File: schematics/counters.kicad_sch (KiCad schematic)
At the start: 50 parts, among them Q1 S8050, U1 74HC14, U10 74HC390, U3 74HC86, U4 74HC4046, U5 74HC390, U6 74HC390, U7 74HC390, U8 LMC555xN, U9 74HC390

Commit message: preliminary PCB design
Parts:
- removed D10, D11, D12, D13, D14, D15, D16, D17, D18, D19, D20, D21, D22, D9: 1N4148, Diode_THT:D_DO-35_SOD27_P7.62mm_Horizontal, symbol Diode:1N4148
- removed R15: 4K7, Resistor_THT:R_Axial_DIN0207_L6.3mm_D2.5mm_P7.62mm_Horizontal, symbol Device:R
- removed R16: 10K, Resistor_THT:R_Axial_DIN0207_L6.3mm_D2.5mm_P7.62mm_Horizontal, symbol Device:R
- removed R17: 1K, Resistor_THT:R_Axial_DIN0207_L6.3mm_D2.5mm_P7.62mm_Horizontal, symbol Device:R
- removed RN2: 4K7, Resistor_THT:R_Array_SIP9, symbol Device:R_Network08_Split
- added C31, C32: 100N, bvclock:THT_Cap, symbol Device:C
- added U31, U33: 74HC08, Package_DIP:DIP-14_W7.62mm, symbol 74xx:74LS08
- added U32: 74HC32, Package_DIP:DIP-14_W7.62mm, symbol 74xx:74LS32
- C10, C11, C12, C13, C14, C15, C16, C17, C18, C19, C8, C9: footprint Capacitor_THT:C_Disc_D5.1mm_W3.2mm_P5.00mm -> bvclock:THT_Cap
- D8: footprint Diode_THT:D_DO-35_SOD27_P7.62mm_Horizontal -> bvclock:THT_D_Vertical
- Q1: value S8050 -> 2N2222
- R10, R11, R12, R13, R7, R8, R9: footprint Resistor_THT:R_Axial_DIN0207_L6.3mm_D2.5mm_P7.62mm_Horizontal -> bvclock:THT_R_Vertical
- R14: value 100R -> 82R; footprint Resistor_THT:R_Axial_DIN0207_L6.3mm_D2.5mm_P7.62mm_Horizontal -> bvclock:THT_R_Vertical
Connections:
- net +3V3: now also R11.2, C31.1, C32.1, U31.14 (VCC), U33.14 (VCC); no longer R11.1
- net GND: now also R8.1, R9.1, C31.2, C32.2, U31.7 (GND), U33.1, U33.2, U33.4, U33.5, U33.7 (GND); no longer R8.2, R9.2
- net HADV: now also U33.10
- net HI2: now also U31.5
- net HI4: now also U31.4
- net MADV: now also U33.13
- net MH1: now also U31.1
- net MH2: now also U31.2
- net SH1: now also U31.9
- net SH2: now also U31.10
- net SRST: now also U32.12
- net at U3.10: now also U33.11
- net at U3.13, U9.14 (2CLR): now also U31.3
- net at U10.13 (2Q_{A}): now also U33.12, U33.9
- net at U3.12: now also U33.8
- net at U10.14 (2CLR), U10.2 (1CLR): now also U31.6
- net at U3.9: now also U31.8, U32.13
- net at RV1.1: now also R11.1; no longer R11.2
- net at D8.1 (K), U1.5: now also R10.1; no longer R10.2
- net at U7.14 (2CLR): now also U32.11
- net at U5.11 (2Q_{B}): now also U31.12
- net at U5.14 (2CLR), U6.1 (1~{CLK}_{A}): now also U31.11
- net at U4.12 (R_{2}): now also R8.2; no longer R8.1
- net at U5.10 (2Q_{C}): now also U31.13
- new net: C8.2, R10.2, R9.2
- no-connect marks 12 -> 14
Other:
- moved on the sheet: C10, C11, C12, C13, C14, C15, C16, C17, C18, C19, C8, C9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

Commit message: fixing DRC violations...
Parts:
- Q1: footprint Package_TO_SOT_THT:TO-92_HandSolder -> bvclock:TO-92_HandSolder
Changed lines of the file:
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@@
 			)
 		)
-		(property "Footprint" "Package_TO_SOT_THT:TO-92_HandSolder"
+		(property "Footprint" "bvclock:TO-92_HandSolder"
 			(at 107.95 135.89 0)
 			(hide yes)

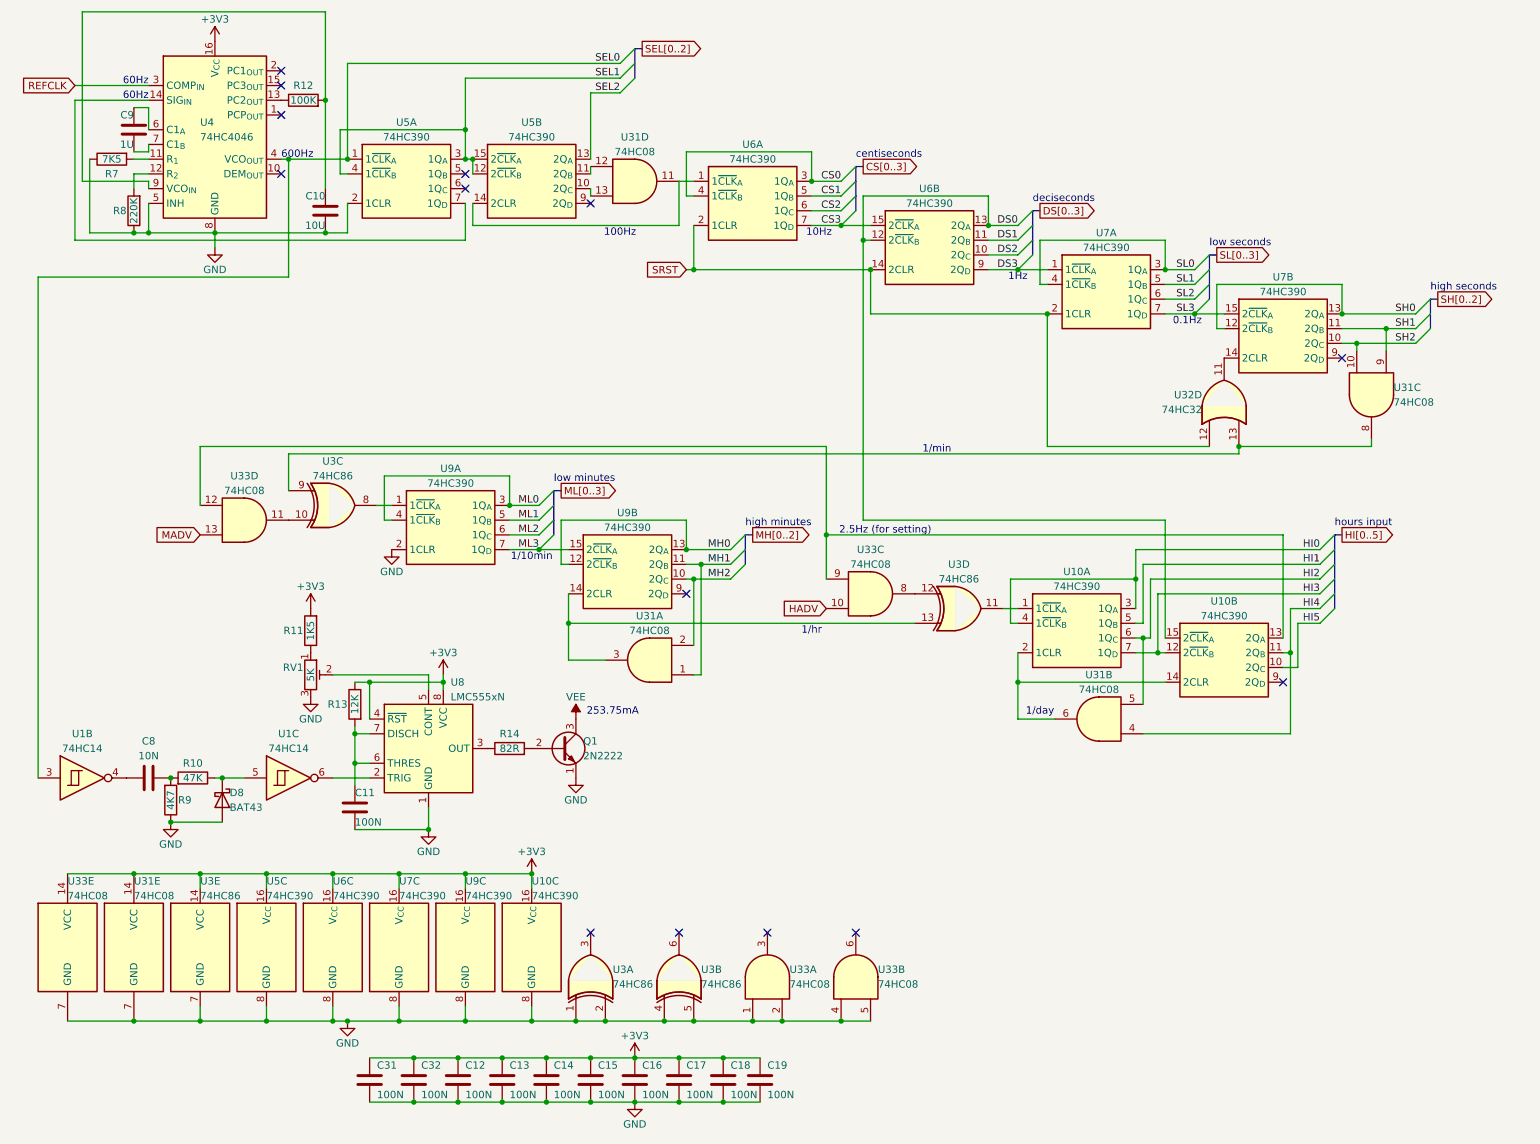
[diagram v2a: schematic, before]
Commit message: passes DRC
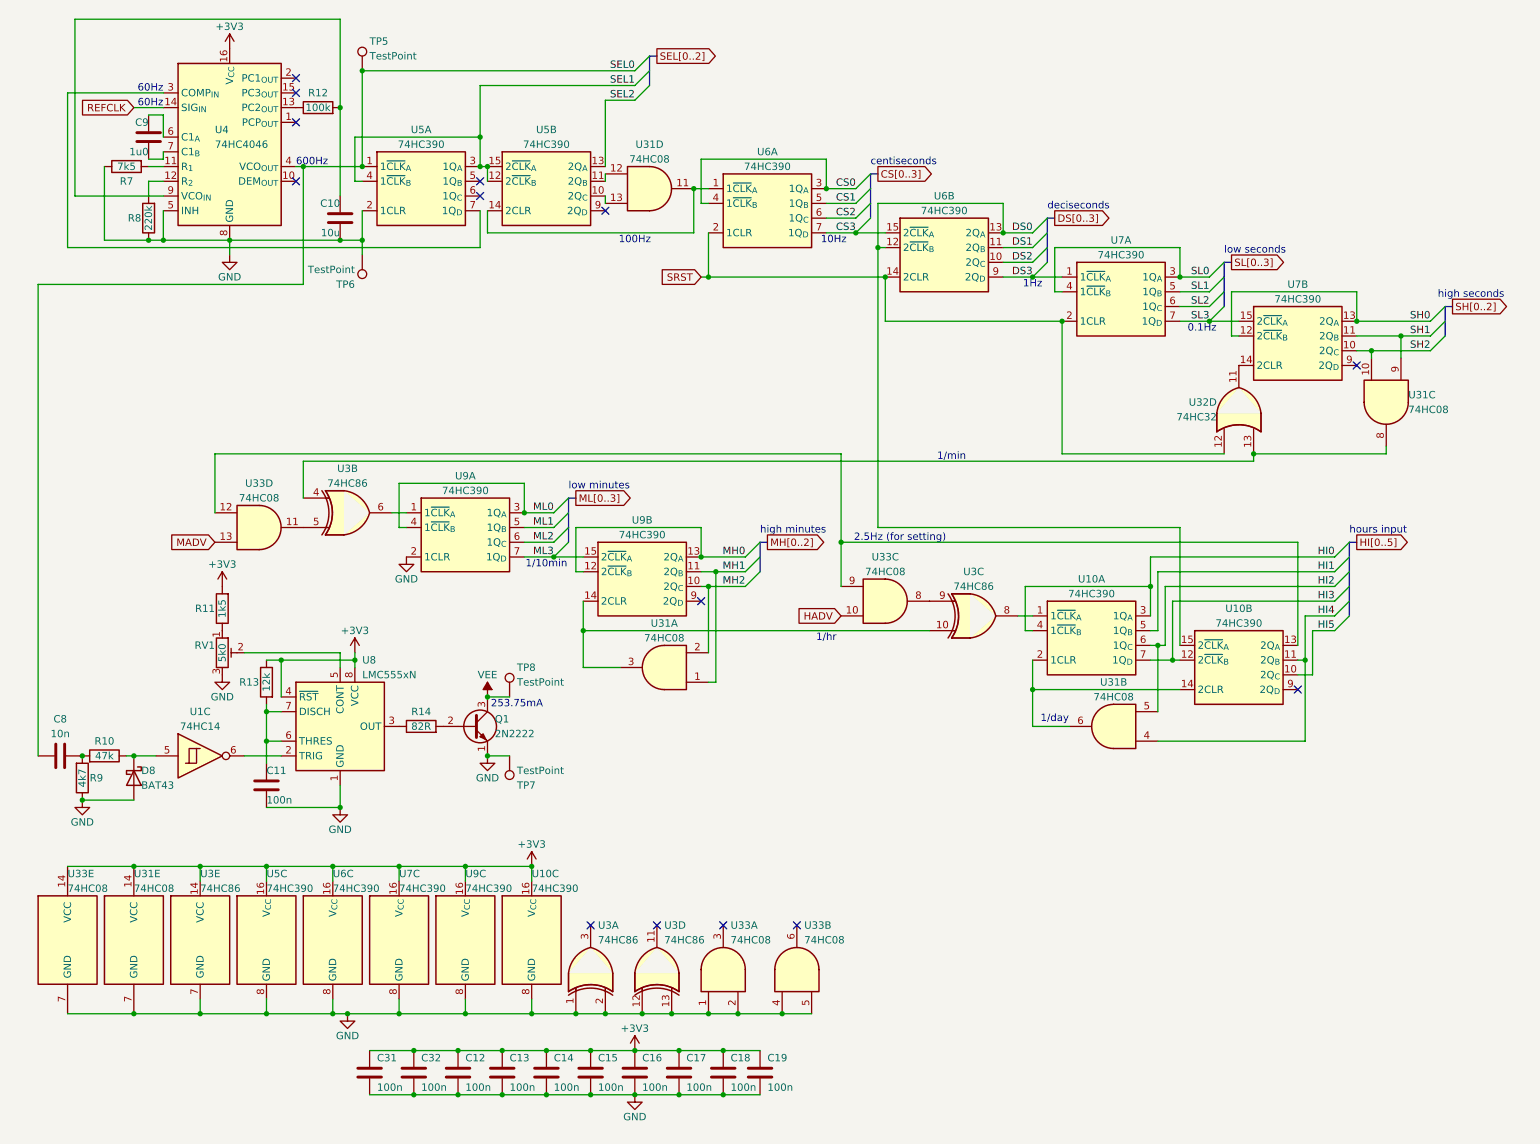
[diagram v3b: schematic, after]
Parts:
- removed unit 2 of U1
- added TP5, TP8: TestPoint, bvclock:TestPoint_THTPad_2.5x2.5mm_Drill1.2mm, symbol Connector:TestPoint
- added TP6, TP7: TestPoint, bvclock:TestPoint_THTPad_D1.0mm_Drill0.5mm, symbol Connector:TestPoint
- C10: value 10U -> 10u
- C11, C12, C13, C14, C15, C16, C17, C18, C19, C31, C32: value 100N -> 100n
- C8: value 10N -> 10n
- C9: value 1U -> 1u0
- R10: value 47K -> 47k
- R11: value 1K5 -> 1k5
- R12: value 100K -> 100k
- R13: value 12K -> 12k
- R7: value 7K5 -> 7k5
- R8: value 220K -> 220k
- R9: value 4K7 -> 4k7
- RV1: value 5K -> 5k0
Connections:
- net GND: now also U3.12, U3.13, TP6.1, TP7.1; no longer U3.4, U3.5
- net REFCLK: now also U4.14 (SIG_{IN}); no longer U4.3 (COMP_{IN})
- net SEL0: now also C8.1, TP5.1
- net VEE: now also TP8.1
- net at U33.8: now also U3.9; no longer U3.12
- net at U31.3, U9.14 (2CLR): now also U3.10; no longer U3.13
- net at U10.1 (1~{CLK}_{A}): now also U3.8; no longer U3.11
- net at U5.7 (1Q_{D}): now also U4.3 (COMP_{IN}); no longer U4.14 (SIG_{IN})
- net at U31.8, U32.13: now also U3.4; no longer U3.9
- net at U33.11: now also U3.5; no longer U3.10
- net at U9.1 (1~{CLK}_{A}): now also U3.6; no longer U3.8
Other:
- moved on the sheet: C10, C11, C12, C13, C14, C15, C16, C17, C18, C19, C31, C32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

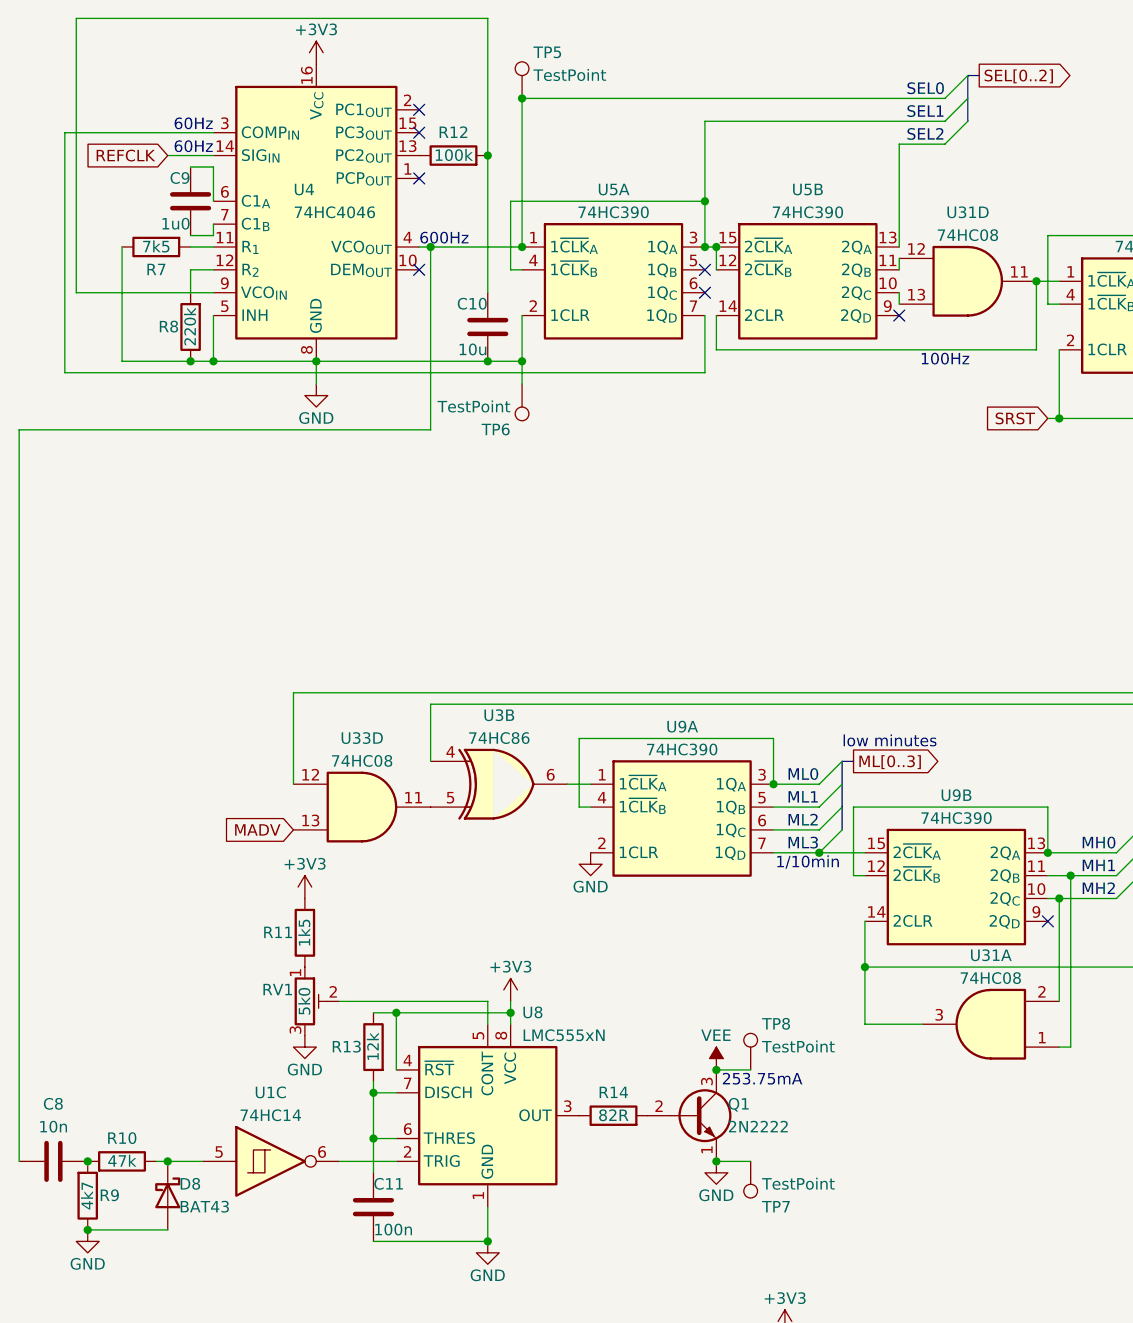
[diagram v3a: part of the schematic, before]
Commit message: switch fix, testpoint for DEMOUT, rearrange resistors
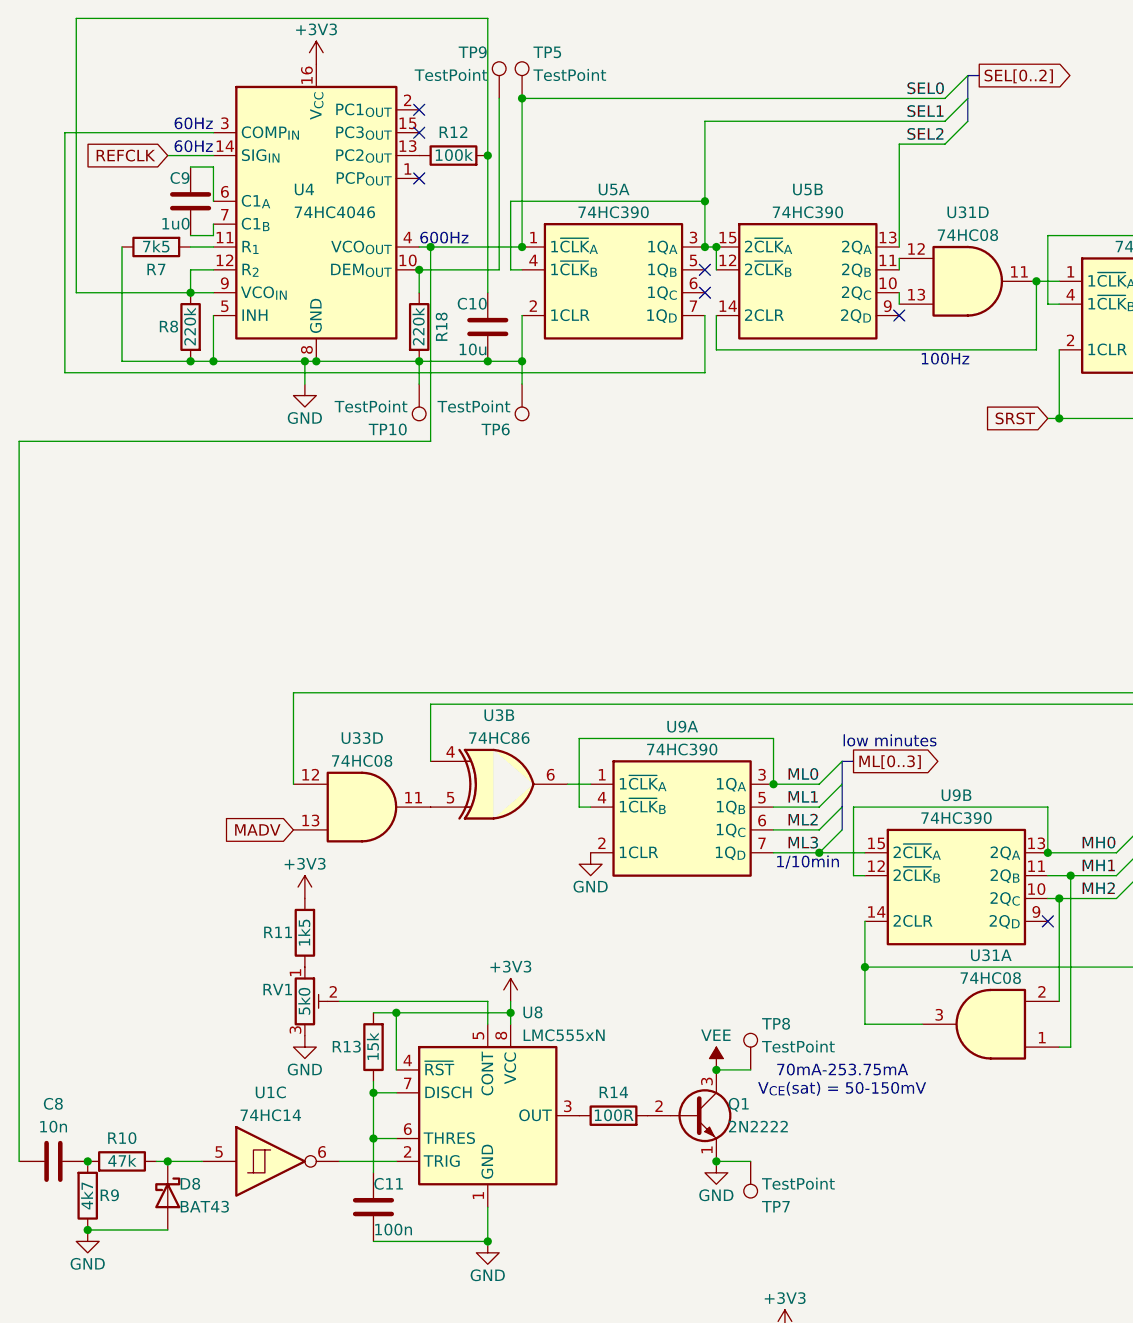
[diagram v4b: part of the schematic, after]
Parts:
- added R18: 220k, bvclock:THT_R_Vertical, symbol Device:R
- added TP10: TestPoint, bvclock:TestPoint_THTPad_D1.0mm_Drill0.5mm, symbol Connector:TestPoint
- added TP9: TestPoint, bvclock:TestPoint_THTPad_2.5x2.5mm_Drill1.2mm, symbol Connector:TestPoint
- R13: value 12k -> 15k
- R14: value 82R -> 100R
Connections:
- net +3V3: now also R13.2; no longer R13.1
- net GND: now also R8.2, R18.2, TP10.1; no longer R8.1
- net at C10.1, R12.2, U4.9 (VCO_{IN}): now also R8.1, U4.12 (R_{2})
- net at C11.1, U8.6 (THRES), U8.7 (DISCH): now also R13.1; no longer R13.2
- net at U4.10 (DEM_{OUT}): now also R18.1, TP9.1
- no-connect marks 14 -> 13
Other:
- note added: "70mA-253.75mA V_{CE}(sat) = 50-150mV"
- note removed: "253.75mA"
- moved on the sheet: R13, R8

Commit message: changed buck converter
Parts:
- removed R11: 1k5, bvclock:THT_R_Vertical, symbol Device:R
- added C42: 22u, Capacitor_THT:CP_Radial_D5.0mm_P2.00mm, symbol Device:C_Polarized
- R13: value 15k -> 3k3
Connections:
- net +3V3: now also RV1.1, C42.1
- net GND: now also C42.2
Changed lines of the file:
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@@
 	)
 	(junction
+		(at 69.85 190.5)
+		(diameter 0)
+		(color 0 0 0 0)
+	)
+	(junction
 		(at 129.54 107.95)
 		(diameter 0)
@@
 	)
 	(junction
+		(at 69.85 198.12)
+		(diameter 0)
+		(color 0 0 0 0)
+	)
+	(junction
 		(at 184.15 128.27)
 		(diameter 0)
@@
 	(wire
 		(pts
+			(xy 63.5 198.12) (xy 69.85 198.12)
+		)
+		(stroke
+			(width 0)
+			(type default)
+		)
+	)
+	(wire
+		(pts
 			(xy 157.48 44.45) (xy 157.48 52.07)
 		)
@@
 	(wire
 		(pts
+			(xy 63.5 190.5) (xy 69.85 190.5)
+		)
+		(stroke
+			(width 0)
+			(type default)
+		)
+	)
+	(wire
+		(pts
 			(xy 110.49 43.18) (xy 110.49 44.45)
 		)
@@
 			)
 		)
-		(property "Value" "15k"
+		(property "Value" "3k3"
 			(at 52.07 127 90)
 			(show_name no)
@@
 	)
 	(symbol
+		(lib_id "Device:C_Polarized")
+		(at 63.5 194.31 0)
+		(mirror y)
+		(unit 1)
+		(body_style 1)
+		(exclude_from_sim no)
+		(in_bom yes)
+		(on_board yes)
+		(in_pos_files yes)
+		(dnp no)
+		(property "Reference" "C42"
+			(at 63.5 191.77 0)
+			(show_name no)
+			(do_not_autoplace no)
+			(effects
+				(font
+					(size 1.27 1.27)
+				)
+				(justify left)
+			)
+		)
+		(property "Value" "22u"
+			(at 63.5 196.85 0)
+			(show_name no)
+			(do_not_autoplace no)
+			(effects
+				(font
+					(size 1.27 1.27)
+				)
+				(justify left)
+			)
+		)
+		(property "Footprint" "Capacitor_THT:CP_Radial_D5.0mm_P2.00mm"
+			(at 62.5348 198.12 0)
+			(hide yes)
+			(show_name no)
+			(do_not_autoplace no)
+			(effects
+				(font
+					(size 1.27 1.27)
+				)
+			)
+		)
+		(property "Datasheet" ""
+			(at 63.5 194.31 0)
+			(hide yes)
+			(show_name no)
+			(do_not_autoplace no)
+			(effects
+				(font
+					(size 1.27 1.27)
+				)
+			)
+		)
+		(property "Description" "Polarized capacitor"
+			(at 63.5 194.31 0)
+			(hide yes)
+			(show_name no)
+			(do_not_autoplace no)
+			(effects
+				(font
+					(size 1.27 1.27)
+				)
+			)
+		)
+		(pin "2"
+		)
+		(pin "1"
+		)
+		(instances
+			(project "bvclock"
+				(path "/c60296a7-2d90-476d-9ba8-593ef9b0941e/1e5cbbe7-ce51-4eb7-9339-265272a6e33a"
+					(reference "C42")
+					(unit 1)
+				)
+			)
+		)
+	)
+	(symbol
 		(lib_id "Connector:TestPoint")
 		(at 93.98 139.7 0)
@@
 	(symbol
 		(lib_id "power:+5V")
-		(at 44.45 110.49 0)
+		(at 44.45 118.11 0)
 		(unit 1)
 		(body_style 1)
@@
 		(dnp no)
 		(property "Reference" "#PWR022"
-			(at 44.45 114.3 0)
+			(at 44.45 121.92 0)
 			(hide yes)
 			(show_name no)
@@
 		)
 		(property "Value" "+3V3"
-			(at 44.45 106.68 0)
+			(at 44.45 114.3 0)
 			(show_name no)
 			(do_not_autoplace no)
@@
 		)
 		(property "Footprint" ""
-			(at 44.45 110.49 0)
+			(at 44.45 118.11 0)
 			(hide yes)
 			(show_name no)
@@
 		)
 		(property "Datasheet" ""
-			(at 44.45 110.49 0)
+			(at 44.45 118.11 0)
 			(hide yes)
 			(show_name no)
@@
 		)
 		(property "Description" "Power symbol creates a global label with name \"+5V\""
-			(at 44.45 110.49 0)
+			(at 44.45 118.11 0)
 			(hide yes)
 			(show_name no)
@@
 					(unit 1)
 				)
-			)
-		)
-	)
-	(symbol
-		(lib_id "Device:R")
-		(at 44.45 114.3 180)
-		(unit 1)
-		(body_style 1)
-		(exclude_from_sim no)
-		(in_bom yes)
-		(on_board yes)
-		(in_pos_files yes)
-		(dnp no)
-		(property "Reference" "R11"
-			(at 43.18 114.3 0)
-			(show_name no)
-			(do_not_autoplace no)
-			(effects
-				(font
-					(size 1.27 1.27)
-				)
-				(justify left)
-			)
-		)
-		(property "Value" "1k5"
-			(at 44.45 114.3 90)
-			(show_name no)
-			(do_not_autoplace no)
-			(effects
-				(font
-					(size 1.27 1.27)
-				)
-			)
-		)
-		(property "Footprint" "bvclock:THT_R_Vertical"
-			(at 46.228 114.3 90)
-			(hide yes)
-			(show_name no)
-			(do_not_autoplace no)
-			(effects
-				(font
-					(size 1.27 1.27)
-				)
-			)
-		)
-		(property "Datasheet" ""
-			(at 44.45 114.3 0)
-			(hide yes)
-			(show_name no)
-			(do_not_autoplace no)
-			(effects
-				(font
-					(size 1.27 1.27)
-				)
-			)
-		)
-		(property "Description" "Resistor"
-			(at 44.45 114.3 0)
-			(hide yes)
-			(show_name no)
-			(do_not_autoplace no)
-			(effects
-				(font
-					(size 1.27 1.27)
-				)
-			)
-		)
-		(pin "1"
-		)
-		(pin "2"
-		)
-		(instances
-			(project "bvclock"
-				(path "/c60296a7-2d90-476d-9ba8-593ef9b0941e/1e5cbbe7-ce51-4eb7-9339-265272a6e33a"
-					(reference "R11")
-					(unit 1)
-				)
